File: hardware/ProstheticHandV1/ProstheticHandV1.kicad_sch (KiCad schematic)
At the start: 25 parts, among them J1 Servo_01, J2 Servo_02, J3 Servo_03, J4 Servo_04, J5 JTAG, J6 Bat_Con, J7 OLED_Disp, J8 EMG_Sensor_01, J9 EMG_Sensor_02, SW1 Button_01, SW2 Button_02, U1 LM7805_TO220, U2 LM7809_TO220, U3 LM7909_TO220

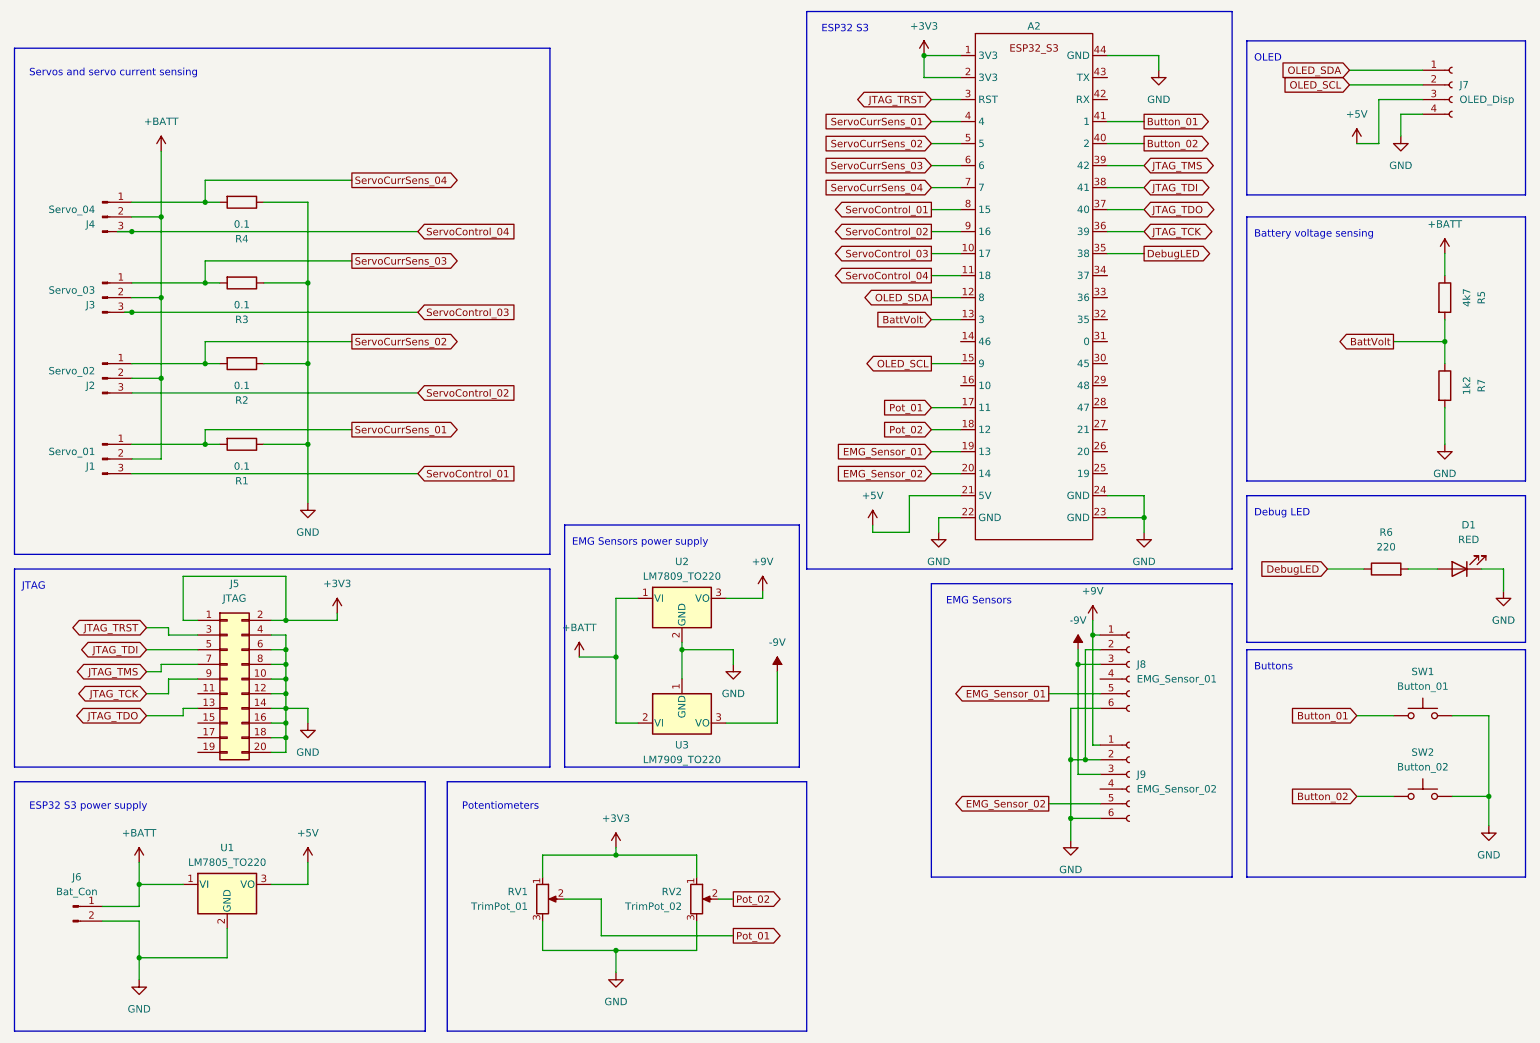
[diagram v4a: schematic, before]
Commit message: Update PCB for hand, completely new design
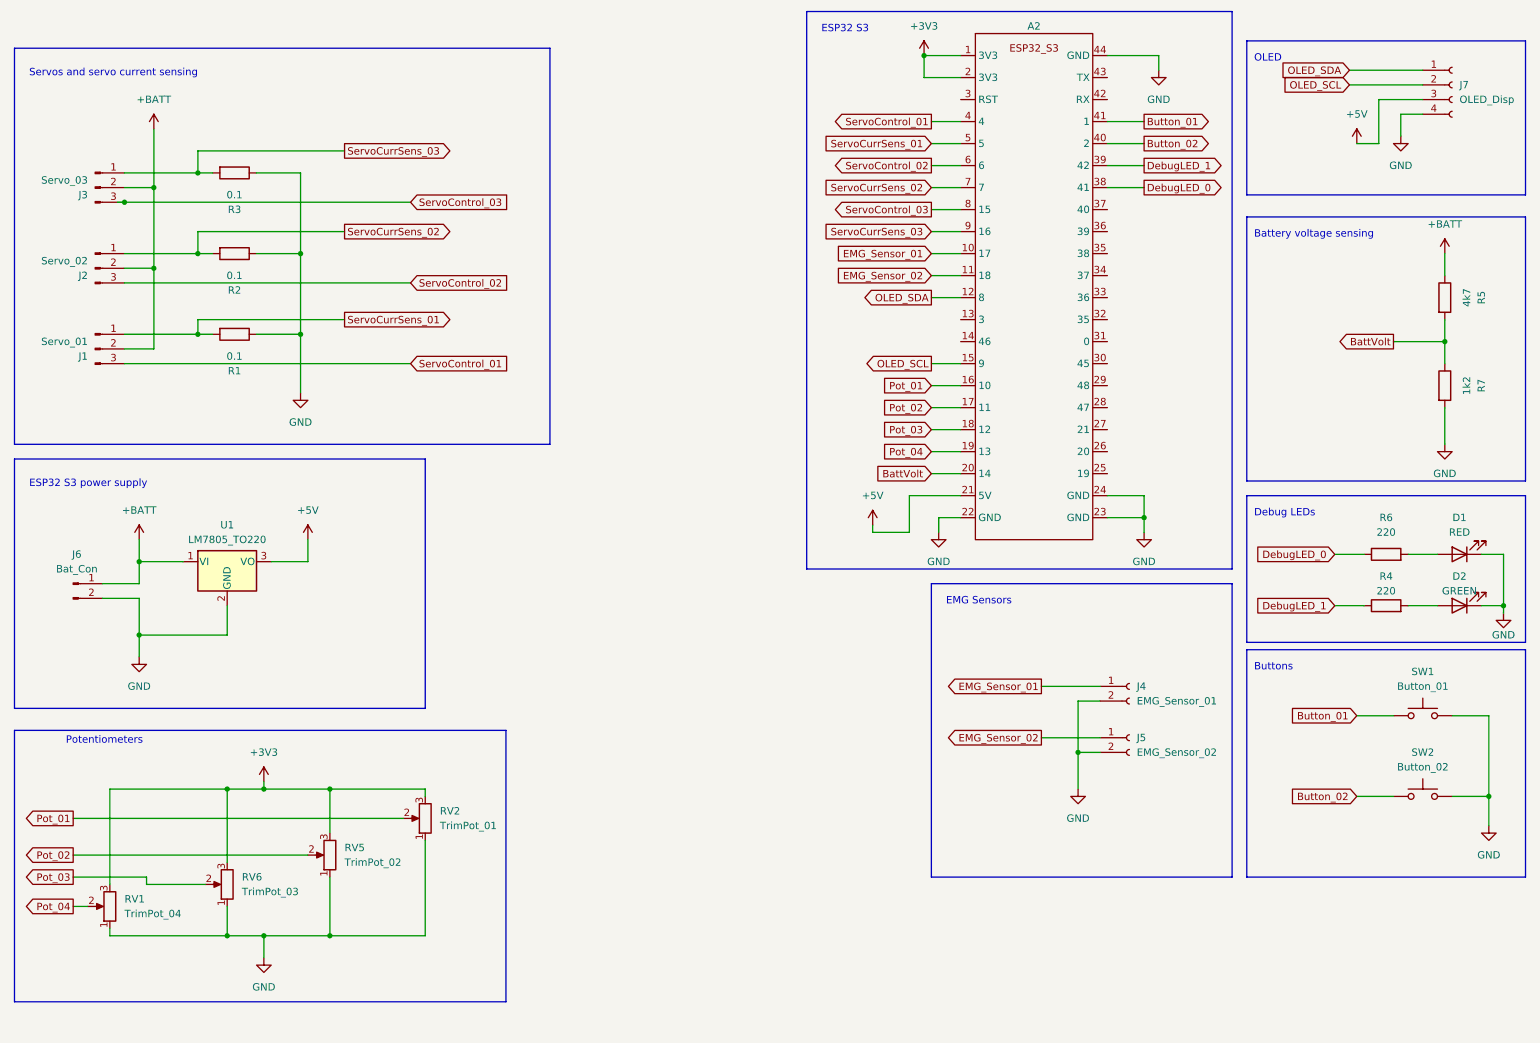
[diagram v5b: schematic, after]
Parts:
- removed J4: Servo_04, Connector_PinHeader_2.54mm:PinHeader_1x03_P2.54mm_Vertical, symbol Connector:Conn_01x03_Pin
- removed J5: JTAG, Connector_PinHeader_2.54mm:PinHeader_2x10_P2.54mm_Vertical, symbol Connector_Generic:Conn_02x10_Odd_Even
- removed J8: EMG_Sensor_01, Connector_PinHeader_2.54mm:PinHeader_1x06_P2.54mm_Vertical, symbol Connector:Conn_01x06_Socket
- removed J9: EMG_Sensor_02, Connector_PinHeader_2.54mm:PinHeader_1x06_P2.54mm_Vertical, symbol Connector:Conn_01x06_Socket
- removed U2: LM7809_TO220, Package_TO_SOT_THT:TO-220-3_Vertical, symbol Regulator_Linear:LM7809_TO220
- removed U3: LM7909_TO220, Package_TO_SOT_THT:TO-220-3_Vertical, symbol Regulator_Linear:LM7909_TO220
- added D2: GREEN, LED_THT:LED_D5.0mm, symbol Device:LED
- added J4: EMG_Sensor_01, Connector_PinSocket_2.54mm:PinSocket_1x02_P2.54mm_Vertical, symbol Connector:Conn_01x02_Socket
- added J5: EMG_Sensor_02, Connector_PinSocket_2.54mm:PinSocket_1x02_P2.54mm_Vertical, symbol Connector:Conn_01x02_Socket
- added RV5: TrimPot_02, Potentiometer_THT:Potentiometer_Alps_RK163_Single_Horizontal, symbol Device:R_Potentiometer
- added RV6: TrimPot_03, Connector_PinHeader_2.54mm:PinHeader_1x03_P2.54mm_Vertical, symbol Device:R_Potentiometer
- A2: footprint MyLibrary:ESP32_S3_DevKitC_V1 -> FootprintLibrary:ESP32S3_DevModule
- R4: value 0.1 -> 220; footprint Resistor_THT:R_Axial_Power_L25.0mm_W9.0mm_P27.94mm -> Resistor_THT:R_Axial_DIN0207_L6.3mm_D2.5mm_P7.62mm_Horizontal
- RV1: value TrimPot_01 -> TrimPot_04; footprint Potentiometer_THT:Potentiometer_Alps_RK163_Single_Horizontal -> Connector_PinHeader_2.54mm:PinHeader_1x03_P2.54mm_Vertical
- RV2: value TrimPot_02 -> TrimPot_01
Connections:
- net ServoControl_04 is gone; now on net EMG_Sensor_02: A2.11 (18)
- net +3V3: now also RV1.3, RV2.3, RV5.3, RV6.3; no longer RV1.1, RV2.1
- net BattVolt: now also A2.20 (14); no longer A2.13 (3)
- net EMG_Sensor_01: now also A2.10 (17), J4.1 (Pin_1); no longer A2.19 (13)
- net EMG_Sensor_02: now also J5.1 (Pin_1); no longer A2.20 (14)
- net GND: now also RV1.1, RV2.1, D2.1 (K), J4.2 (Pin_2), J5.2 (Pin_2), RV5.1, RV6.1; no longer R4.1, RV1.3, RV2.3
- net Pot_01: now also A2.16 (10), RV2.2; no longer A2.17 (11), RV1.2
- net Pot_02: now also A2.17 (11), RV5.2; no longer A2.18 (12), RV2.2
- net ServoControl_01: now also A2.4; no longer A2.8 (15)
- net ServoControl_02: now also A2.6; no longer A2.9 (16)
- net ServoControl_03: now also A2.8 (15); no longer A2.10 (17)
- net ServoCurrSens_01: now also A2.5; no longer A2.4
- net ServoCurrSens_02: now also A2.7; no longer A2.5
- net ServoCurrSens_03: now also A2.9 (16); no longer A2.6
- net DebugLED: no longer names the net of A2.35 (38)
- net DebugLED: no longer R6.1
- net JTAG_TCK: no longer names the net of A2.36 (39)
- net JTAG_TDI renamed DebugLED_0
- net DebugLED_0: now also R6.1
- net JTAG_TDO: no longer names the net of A2.37 (40)
- net JTAG_TMS renamed DebugLED_1
- net DebugLED_1: now also R4.1
- net JTAG_TRST: no longer names the net of A2.3 (RST)
- net ServoCurrSens_04: no longer names the net of R4.2
- net ServoCurrSens_04: now also D2.2 (A); no longer A2.7
- new net Pot_03: A2.18 (12), RV6.2
- new net Pot_04: A2.19 (13), RV1.2
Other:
- note added: "Debug LEDs"
- note removed: "Debug LED"
- note removed: "EMG Sensors power supply"
- note removed: "JTAG"
- moved on the sheet: D1, J1, J2, J3, J6, R1, R2, R3, R6, RV1, RV2, U1

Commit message: Update code in main branch a bit
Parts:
- added SW3: SW_Boostrap, Button_Switch_THT:SW_DIP_SPSTx04_Slide_9.78x12.34mm_W7.62mm_P2.54mm, symbol Switch:SW_DIP_x04
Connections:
- net DebugLED_0: now also A2.34 (37); no longer A2.38 (41)
- net DebugLED_1: now also A2.35 (38); no longer A2.39 (42)
- net GND: now also SW3.5, SW3.6, SW3.7, SW3.8
- net Boostrap_03: now reaches A2.36 (39)
- net Boostrap_03: now also SW3.4
- net Boostrap_02: now reaches A2.37 (40)
- net Boostrap_02: now also SW3.3
- new net Boostrap_00: A2.39 (42), SW3.1
- new net Boostrap_01: A2.38 (41), SW3.2
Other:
- note added: "DIP Bootstrap Switches"

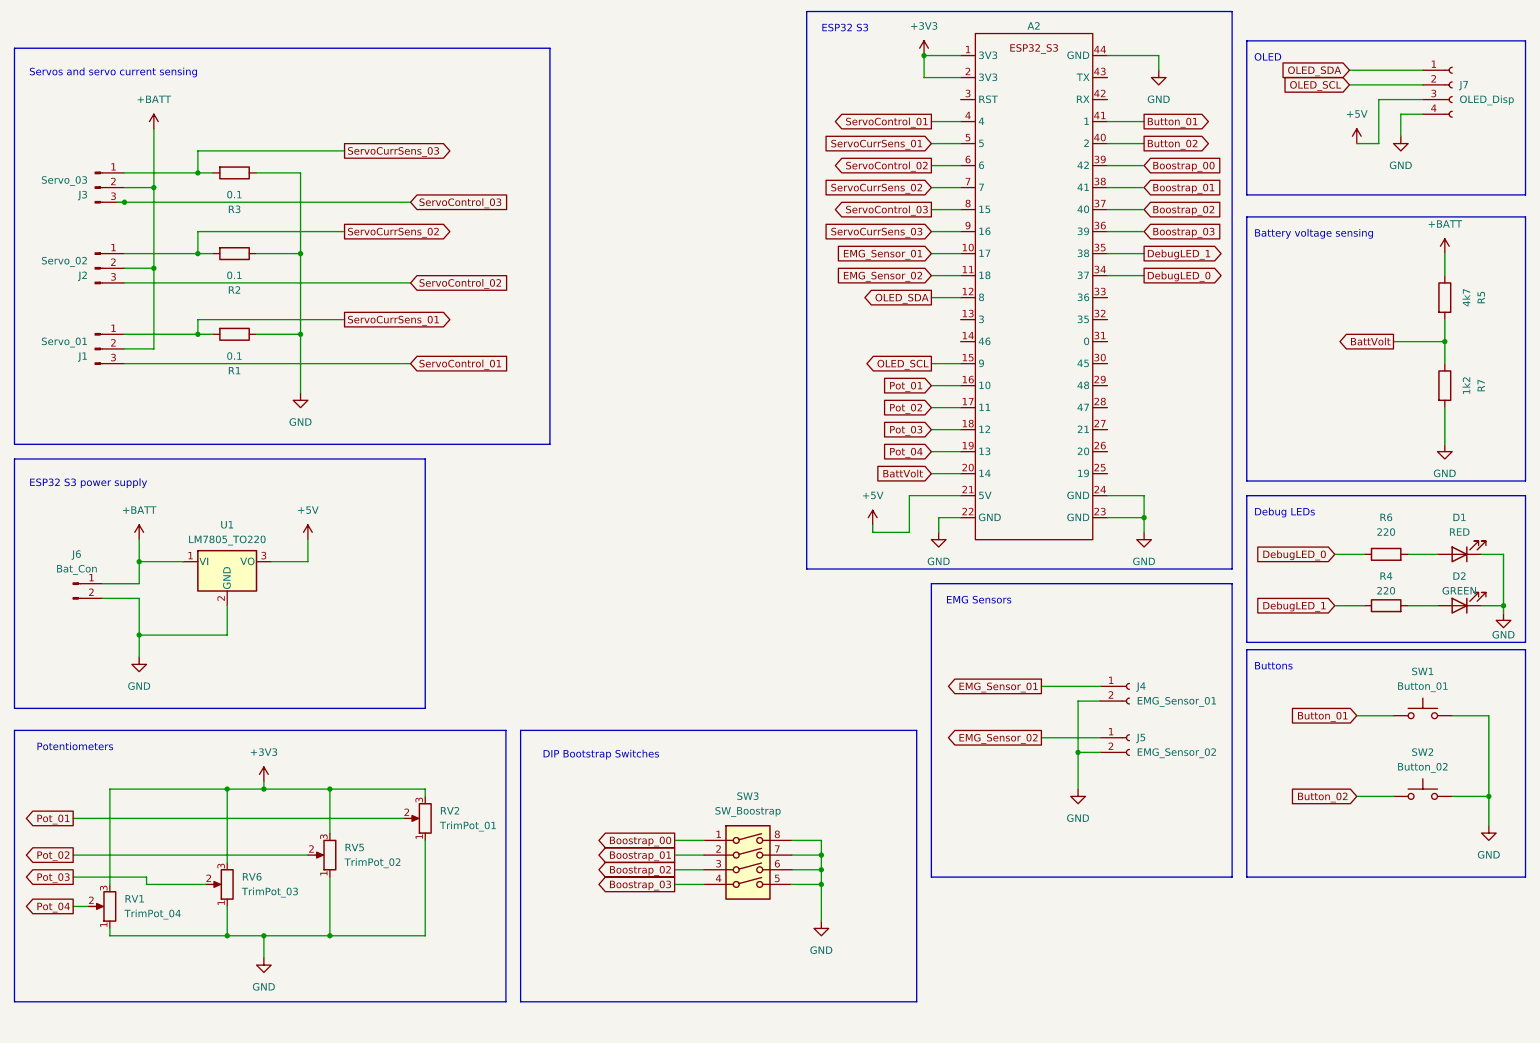
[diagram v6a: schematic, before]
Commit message: Update button driver and schematic names
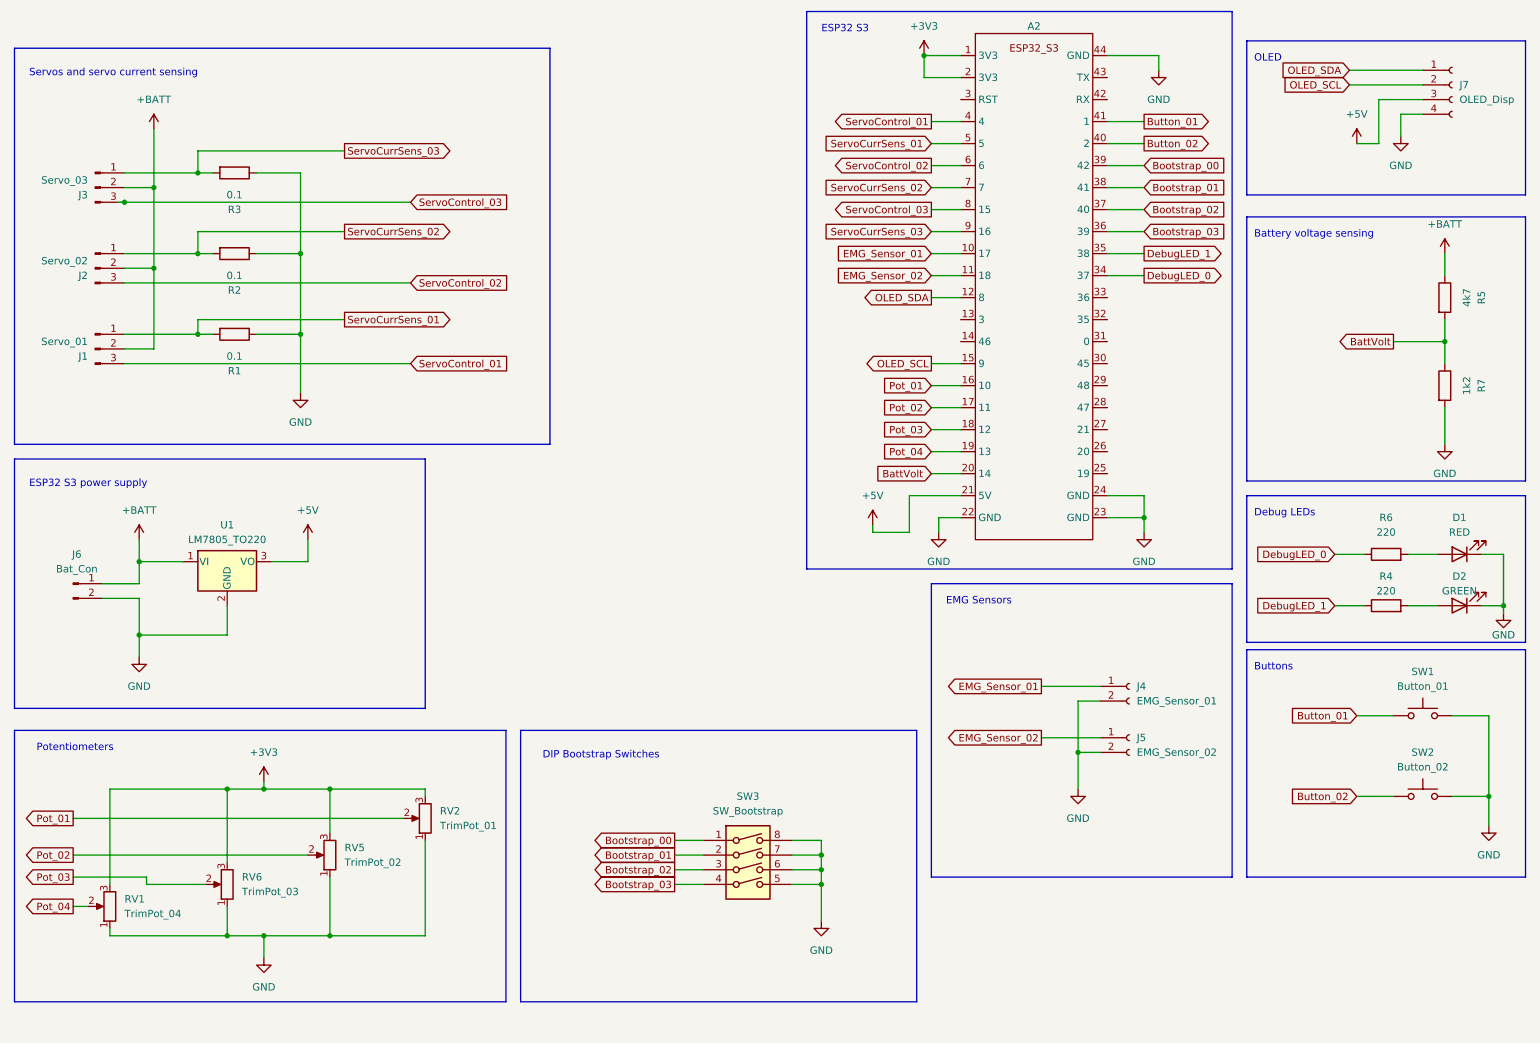
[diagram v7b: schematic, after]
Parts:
- SW3: value SW_Boostrap -> SW_Bootstrap
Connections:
- net Boostrap_00 renamed Bootstrap_00
- net Boostrap_01 renamed Bootstrap_01
- net Boostrap_02 renamed Bootstrap_02
- net Boostrap_03 renamed Bootstrap_03
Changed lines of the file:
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@@
     )
   )
-  (global_label "Boostrap_01" (shape input) (at 214.63 44.45 0) (fields_autoplaced)
-    (effects (font (size 1.27 1.27)) (justify left))
-    (property "Intersheetrefs" "${INTERSHEET_REFS}" (at 229.4078 44.45 0)
+  (global_label "Bootstrap_01" (shape input) (at 214.63 44.45 0) (fields_autoplaced)
+    (effects (font (size 1.27 1.27)) (justify left))
+    (property "Intersheetrefs" "${INTERSHEET_REFS}" (at 230.1335 44.45 0)
       (effects (font (size 1.27 1.27)) (justify left) hide)
     )
@@
     )
   )
-  (global_label "Boostrap_00" (shape input) (at 214.63 40.64 0) (fields_autoplaced)
-    (effects (font (size 1.27 1.27)) (justify left))
-    (property "Intersheetrefs" "${INTERSHEET_REFS}" (at 229.4078 40.64 0)
-      (effects (font (size 1.27 1.27)) (justify left) hide)
-    )
-  )
-  (global_label "Boostrap_01" (shape output) (at 133.35 160.02 180) (fields_autoplaced)
-    (effects (font (size 1.27 1.27)) (justify right))
-    (property "Intersheetrefs" "${INTERSHEET_REFS}" (at 118.5722 160.02 0)
+  (global_label "Bootstrap_00" (shape input) (at 214.63 40.64 0) (fields_autoplaced)
+    (effects (font (size 1.27 1.27)) (justify left))
+    (property "Intersheetrefs" "${INTERSHEET_REFS}" (at 230.1335 40.64 0)
+      (effects (font (size 1.27 1.27)) (justify left) hide)
+    )
+  )
+  (global_label "Bootstrap_01" (shape output) (at 133.35 160.02 180) (fields_autoplaced)
+    (effects (font (size 1.27 1.27)) (justify right))
+    (property "Intersheetrefs" "${INTERSHEET_REFS}" (at 117.8465 160.02 0)
       (effects (font (size 1.27 1.27)) (justify right) hide)
     )
@@
     )
   )
-  (global_label "Boostrap_03" (shape input) (at 214.63 52.07 0) (fields_autoplaced)
-    (effects (font (size 1.27 1.27)) (justify left))
-    (property "Intersheetrefs" "${INTERSHEET_REFS}" (at 229.4078 52.07 0)
-      (effects (font (size 1.27 1.27)) (justify left) hide)
-    )
-  )
-  (global_label "Boostrap_02" (shape output) (at 133.35 162.56 180) (fields_autoplaced)
-    (effects (font (size 1.27 1.27)) (justify right))
-    (property "Intersheetrefs" "${INTERSHEET_REFS}" (at 118.5722 162.56 0)
+  (global_label "Bootstrap_03" (shape input) (at 214.63 52.07 0) (fields_autoplaced)
+    (effects (font (size 1.27 1.27)) (justify left))
+    (property "Intersheetrefs" "${INTERSHEET_REFS}" (at 230.1335 52.07 0)
+      (effects (font (size 1.27 1.27)) (justify left) hide)
+    )
+  )
+  (global_label "Bootstrap_02" (shape output) (at 133.35 162.56 180) (fields_autoplaced)
+    (effects (font (size 1.27 1.27)) (justify right))
+    (property "Intersheetrefs" "${INTERSHEET_REFS}" (at 117.8465 162.56 0)
       (effects (font (size 1.27 1.27)) (justify right) hide)
     )
@@
     )
   )
-  (global_label "Boostrap_00" (shape output) (at 133.35 157.48 180) (fields_autoplaced)
-    (effects (font (size 1.27 1.27)) (justify right))
-    (property "Intersheetrefs" "${INTERSHEET_REFS}" (at 118.5722 157.48 0)
+  (global_label "Bootstrap_00" (shape output) (at 133.35 157.48 180) (fields_autoplaced)
+    (effects (font (size 1.27 1.27)) (justify right))
+    (property "Intersheetrefs" "${INTERSHEET_REFS}" (at 117.8465 157.48 0)
       (effects (font (size 1.27 1.27)) (justify right) hide)
     )
@@
     )
   )
-  (global_label "Boostrap_02" (shape input) (at 214.63 48.26 0) (fields_autoplaced)
-    (effects (font (size 1.27 1.27)) (justify left))
-    (property "Intersheetrefs" "${INTERSHEET_REFS}" (at 229.4078 48.26 0)
+  (global_label "Bootstrap_02" (shape input) (at 214.63 48.26 0) (fields_autoplaced)
+    (effects (font (size 1.27 1.27)) (justify left))
+    (property "Intersheetrefs" "${INTERSHEET_REFS}" (at 230.1335 48.26 0)
       (effects (font (size 1.27 1.27)) (justify left) hide)
     )
@@
     )
   )
-  (global_label "Boostrap_03" (shape output) (at 133.35 165.1 180) (fields_autoplaced)
-    (effects (font (size 1.27 1.27)) (justify right))
-    (property "Intersheetrefs" "${INTERSHEET_REFS}" (at 118.5722 165.1 0)
+  (global_label "Bootstrap_03" (shape output) (at 133.35 165.1 180) (fields_autoplaced)
+    (effects (font (size 1.27 1.27)) (justify right))
+    (property "Intersheetrefs" "${INTERSHEET_REFS}" (at 117.8465 165.1 0)
       (effects (font (size 1.27 1.27)) (justify right) hide)
     )
@@
       (effects (font (size 1.27 1.27)))
     )
-    (property "Value" "SW_Boostrap" (at 146.05 152.4 0)
-      (effects (font (size 1.27 1.27)))
-    )
+    (property "Value" "SW_Bootstrap" (at 146.05 152.4 0)
+      (effects (font (size 1.27 1.27)))
+    )
